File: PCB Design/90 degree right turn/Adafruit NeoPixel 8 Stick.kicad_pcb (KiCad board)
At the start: 2 copper layers, 24.4 x 23.9 mm, 5 parts, among them CN1 1X4SMT, CN2 1X4SMT

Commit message: arrows
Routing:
- net GND: vias 0 -> 1
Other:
- board text removed: "DIN"
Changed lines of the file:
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@@
       (net 2 "GND") (pinfunction "4") (pintype "bidirectional") (solder_mask_margin 0.1016))
   )
+  (gr_line (start 138.176 113.538) (end 135.128 113.538) (layer "B.SilkS") (width 0.12))
+  (gr_line (start 138.176 110.49) (end 138.176 113.538) (layer "B.SilkS") (width 0.12))
+  (gr_line (start 135.128 113.538) (end 138.176 113.538) (layer "B.SilkS") (width 0.12))
+  (gr_line (start 131.318 106.68) (end 138.176 113.538) (layer "B.SilkS") (width 0.12))
   (gr_line (start 131.064 113.792) (end 122.428 113.792) (layer "Edge.Cuts") (width 0.05))
   (gr_line (start 131.064 122.428) (end 131.064 113.792) (layer "Edge.Cuts") (width 0.05))
@@
     (effects (font (size 1.143 1.143) (thickness 0.127)) (justify left bottom mirror))
   )
-  (gr_text "4-7VDC" (at 128.9812 107.0864) (layer "B.SilkS")
-    (effects (font (size 1.143 1.143) (thickness 0.127)) (justify right top mirror))
-  )
   (gr_text "DOUT" (at 155.194 131.4704 270) (layer "B.SilkS")
     (effects (font (size 1.143 1.143) (thickness 0.127)) (justify left bottom mirror))
@@
     (effects (font (size 1.143 1.143) (thickness 0.127)) (justify left bottom mirror))
   )
-  (gr_text "DIN" (at 128.9812 105.0544) (layer "B.SilkS")
-    (effects (font (size 1.143 1.143) (thickness 0.127)) (justify right top mirror))
-  )
   (gr_text "GND" (at 157.734 131.4704 270) (layer "B.SilkS")
     (effects (font (size 1.143 1.143) (thickness 0.127)) (justify left bottom mirror))
-  )
-  (gr_text "GND" (at 128.9812 102.5144) (layer "B.SilkS")
-    (effects (font (size 1.143 1.143) (thickness 0.127)) (justify right top mirror))
-  )
-  (gr_text "GND" (at 128.9812 109.1184) (layer "B.SilkS")
-    (effects (font (size 1.143 1.143) (thickness 0.127)) (justify right top mirror))
   )
   (segment (start 129.286 109.22) (end 134.112 114.046) (width 0.25) (layer "F.Cu") (net 1))
@@
   (via (at 137.084 119.798) (size 0.8) (drill 0.4) (layers "F.Cu" "B.Cu") (net 1))
   (via (at 127 108.458) (size 0.8) (drill 0.4) (layers "F.Cu" "B.Cu") (net 1))
+  (via (at 133.35 111.76) (size 0.8) (drill 0.4) (layers "F.Cu" "B.Cu") (free) (net 2))
   (via (at 140.462 119.634) (size 0.8) (drill 0.4) (layers "F.Cu" "B.Cu") (net 3))
   (segment (start 127 104.648) (end 127 106.592) (width 0.25) (layer "F.Cu") (net 4))

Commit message: 6 pin
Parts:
- moved D3 4.54 mm to (140.7, 121.9)
- moved D2 4.19 mm to (134.6, 113.8)
- moved CN1 3.42 mm to (140.1, 121.7)
- moved D1 1.83 mm to (126.5, 108.0)
- moved CN2 0.52 mm to (126.9, 107.4)
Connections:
- CN1 pad 1: GND -> Net-(CN1-Pad1)
- CN1 pad 3: +5V -> GND
- CN1 pad 4: GND -> Net-(D3-Pad2)
- D3 pad 2: Net-(CN1-Pad2) -> Net-(D3-Pad2)
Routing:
- net Net-(CN1-Pad1): track 0.00 -> 33.4 mm
- net Net-(CN1-Pad2): track 0.00 -> 30.2 mm, vias 1 -> 0
- net +5V: track 22.5 -> 28.2 mm
- net Net-(D3-Pad2): track 0.00 -> 4.87 mm, vias 0 -> 1
- net Net-(CN2-Pad3): track 3.97 -> 0.00 mm
- net Net-(D1-Pad2): track 5.26 -> 8.01 mm
- net Net-(D2-Pad2): track 5.16 -> 5.75 mm
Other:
- board size 24.4 x 23.9 mm -> 28.6 x 28.6 mm
- board text removed: "4-7VDC"
- board text removed: "DOUT"
- board text removed: "GND"

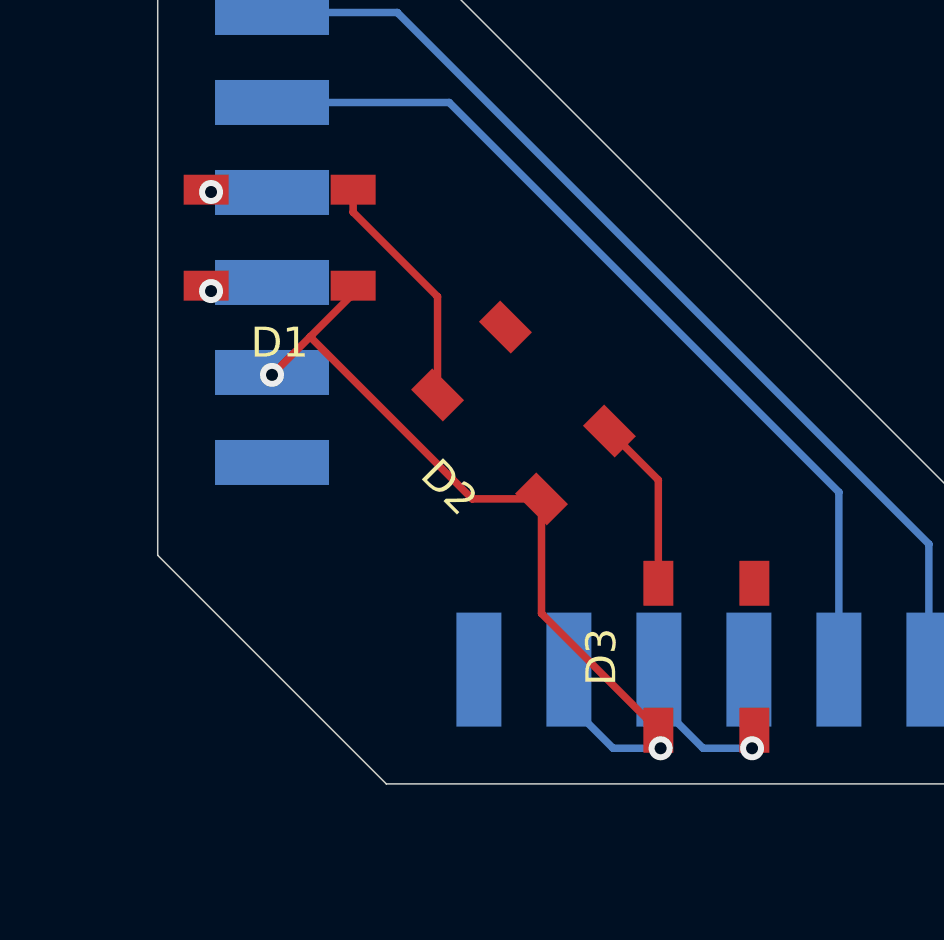
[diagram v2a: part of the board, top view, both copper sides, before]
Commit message: move vias off pads
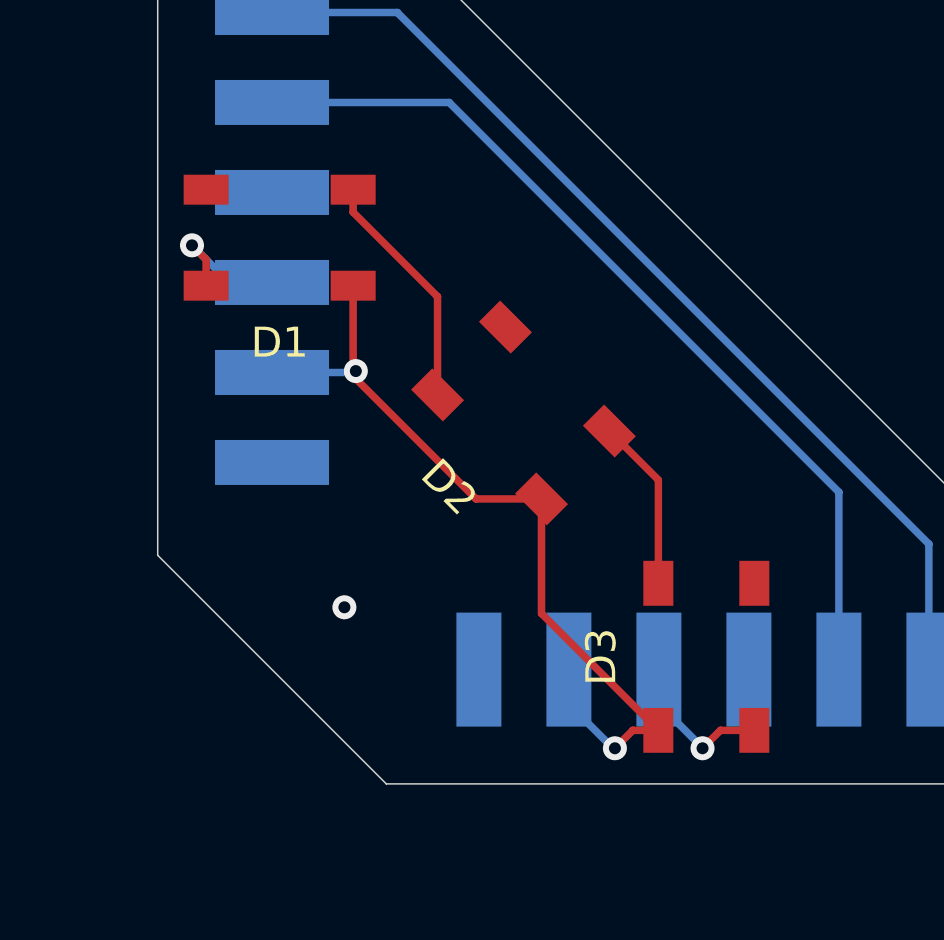
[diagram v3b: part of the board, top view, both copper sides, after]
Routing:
- net Net-(CN2-Pad3): track 0.00 -> 4.72 mm
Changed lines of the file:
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@@
   (gr_line (start 122.428 118.536) (end 130.048 126.155999) (layer "Edge.Cuts") (width 0.05))
   (gr_line (start 130.048 97.536) (end 151.048 118.535998) (layer "Edge.Cuts") (width 0.05))
-  (segment (start 132.911782 116.655782) (end 127.508 111.252) (width 0.25) (layer "F.Cu") (net 1))
-  (segment (start 135.221041 116.655782) (end 132.911782 116.655782) (width 0.25) (layer "F.Cu") (net 1))
-  (segment (start 128.942 109.818) (end 128.942 109.55) (width 0.25) (layer "F.Cu") (net 1))
-  (segment (start 126.238 112.522) (end 127.508 111.252) (width 0.25) (layer "F.Cu") (net 1))
+  (segment (start 133.038782 116.655782) (end 129.032 112.649) (width 0.25) (layer "F.Cu") (net 1))
+  (segment (start 129.032 112.649) (end 129.032 112.395) (width 0.25) (layer "F.Cu") (net 1))
+  (segment (start 135.221041 116.655782) (end 133.038782 116.655782) (width 0.25) (layer "F.Cu") (net 1))
+  (segment (start 139.116 124.37) (end 138.266 124.37) (width 0.25) (layer "F.Cu") (net 1))
+  (segment (start 128.942 112.305) (end 129.032 112.395) (width 0.25) (layer "F.Cu") (net 1))
+  (segment (start 128.942 109.55) (end 128.942 112.305) (width 0.25) (layer "F.Cu") (net 1))
   (segment (start 135.221041 120.475041) (end 139.116 124.37) (width 0.25) (layer "F.Cu") (net 1))
-  (segment (start 127.508 111.252) (end 128.942 109.818) (width 0.25) (layer "F.Cu") (net 1))
+  (segment (start 138.266 124.37) (end 137.668 124.968) (width 0.25) (layer "F.Cu") (net 1))
   (segment (start 135.221041 116.655782) (end 135.221041 120.475041) (width 0.25) (layer "F.Cu") (net 1))
-  (via (at 126.238 112.522) (size 0.8) (drill 0.4) (layers "F.Cu" "B.Cu") (net 1))
-  (via (at 139.192 124.968) (size 0.8) (drill 0.4) (layers "F.Cu" "B.Cu") (net 1))
-  (segment (start 139.192 124.968) (end 137.606 124.968) (width 0.25) (layer "B.Cu") (net 1))
+  (via (at 129.032 112.395) (size 0.8) (drill 0.4) (layers "F.Cu" "B.Cu") (net 1))
+  (via (at 137.668 124.968) (size 0.8) (drill 0.4) (layers "F.Cu" "B.Cu") (net 1))
   (segment (start 136.134 123.496) (end 136.134 122.346) (width 0.25) (layer "B.Cu") (net 1))
+  (segment (start 128.985 112.442) (end 129.032 112.395) (width 0.25) (layer "B.Cu") (net 1))
   (segment (start 137.606 124.968) (end 136.134 123.496) (width 0.25) (layer "B.Cu") (net 1))
-  (via (at 124.206 106.426) (size 0.8) (drill 0.4) (layers "F.Cu" "B.Cu") (net 2))
+  (segment (start 126.238 112.442) (end 128.985 112.442) (width 0.25) (layer "B.Cu") (net 1))
+  (via (at 128.651 120.269) (size 0.8) (drill 0.4) (layers "F.Cu" "B.Cu") (free) (net 2))
   (segment (start 145.134 116.432) (end 145.134 122.346) (width 0.25) (layer "B.Cu") (net 3))
   (segment (start 132.144 103.442) (end 145.134 116.432) (width 0.25) (layer "B.Cu") (net 3))
   (segment (start 126.238 103.442) (end 132.144 103.442) (width 0.25) (layer "B.Cu") (net 3))
-  (via (at 124.206 109.728) (size 0.8) (drill 0.4) (layers "F.Cu" "B.Cu") (net 4))
+  (segment (start 124.042 109.55) (end 124.042 108.675) (width 0.25) (layer "F.Cu") (net 4))
+  (segment (start 124.042 108.675) (end 123.571 108.204) (width 0.25) (layer "F.Cu") (net 4))
+  (via (at 123.571 108.204) (size 0.8) (drill 0.4) (layers "F.Cu" "B.Cu") (net 4))
+  (segment (start 126.238 109.442) (end 124.809 109.442) (width 0.25) (layer "B.Cu") (net 4))
+  (segment (start 124.809 109.442) (end 123.571 108.204) (width 0.25) (layer "B.Cu") (net 4))
   (segment (start 131.756218 109.914218) (end 131.756218 113.190959) (width 0.25) (layer "F.Cu") (net 5))
   (segment (start 128.942 106.35) (end 128.942 107.1) (width 0.25) (layer "F.Cu") (net 5))
@@
   (segment (start 137.483782 114.393041) (end 139.116 116.025259) (width 0.25) (layer "F.Cu") (net 6))
   (segment (start 139.116 116.025259) (end 139.116 119.47) (width 0.25) (layer "F.Cu") (net 6))
-  (via (at 142.24 124.968) (size 0.8) (drill 0.4) (layers "F.Cu" "B.Cu") (net 7))
-  (segment (start 142.24 124.968) (end 140.606 124.968) (width 0.25) (layer "B.Cu") (net 7))
+  (segment (start 142.316 124.37) (end 141.187 124.37) (width 0.25) (layer "F.Cu") (net 7))
+  (segment (start 141.187 124.37) (end 140.589 124.968) (width 0.25) (layer "F.Cu") (net 7))
+  (via (at 140.589 124.968) (size 0.8) (drill 0.4) (layers "F.Cu" "B.Cu") (net 7))
   (segment (start 140.606 124.968) (end 139.134 123.496) (width 0.25) (layer "B.Cu") (net 7))
   (segment (start 139.134 123.496) (end 139.134 122.346) (width 0.25) (layer "B.Cu") (net 7))
